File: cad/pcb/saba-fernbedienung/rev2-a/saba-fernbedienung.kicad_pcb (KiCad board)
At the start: 4 copper layers, 100 x 81.8 mm, 236 parts, among them J201 Conn_ARM_JTAG_SWD_10, J301 Conn_01x04, J302 Conn_01x04, J303 Micro_SD_Card, J304 Conn_01x04, J305 AudioJack3, J306 Conn_01x02, J307 Conn_01x04, J308 Conn_01x01, J309 Conn_01x01, J310 Conn_01x01, J311 Conn_01x04, J312 Conn_01x08, J313 USB_C_Receptacle_USB2.0, K601 G6K-2, K602 G6K-2, K603 G6K-2, K604 G6K-2, K605 G6K-2, K606 G6K-2, K607 EC2-5TNU, Q201 BC856, Q601 BC846, Q602 BC846, Q603 BC846, Q604 BC846, Q605 BC846, Q606 BC846, Q607 BC846, U201 DOIT-DEVKITV1-ESP32-WROOM-32, U301 TSOP31238, U401 TEC2-0911, U402 1117 1.8V, U403 1117 3.3V, U501 ADA4522-2, U502 LM339, U503 LTV-357T, U504 LTV-357T, U505 LTV-357T, U601 LTV-357T, U701 AD8656, U702 VS1053, Y701 12,288MHz

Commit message: ToDo-s bearbeitet
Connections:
- D601 pad 2: /Fernbedienung/Relais_Suchlauf_R -> /Fernbedienung/Relais_Suchlauf_L
- D606 pad 2: /Fernbedienung/Relais_Suchlauf_L -> /Fernbedienung/Relais_Suchlauf_R
- J312 pad 1: SPI_CS_LCD -> (no net)
- J312 pad 8: LCD_A0 -> (no net)
- K601 pad 2: /Fernbedienung/Relais_Leise -> /Fernbedienung/Relais_Laut
- K602 pad 8: /Fernbedienung/Relais_Suchlauf_R -> /Fernbedienung/Relais_Suchlauf_L
- K603 pad 2: /Fernbedienung/Relais_Laut -> /Fernbedienung/Relais_Leise
- K605 pad 8: /Fernbedienung/Relais_Suchlauf_L -> /Fernbedienung/Relais_Suchlauf_R
- Q601 pad 3: /Fernbedienung/Relais_Suchlauf_R -> /Fernbedienung/Relais_Suchlauf_L
- Q602 pad 3: /Fernbedienung/Relais_Laut -> /Fernbedienung/Relais_Leise
- Q603 pad 3: /Fernbedienung/Relais_Suchlauf_L -> /Fernbedienung/Relais_Suchlauf_R
- Q604 pad 3: /Fernbedienung/Relais_Leise -> /Fernbedienung/Relais_Laut
- R203 pad 2: Net-(R203-Pad2) -> (no net)
- R206 pad 2: SABA_Leise -> SABA_Laut
- R207 pad 2: SABA_Suchlauf_L -> SABA_Suchlauf_R
- R208 pad 2: SABA_Suchlauf_R -> SABA_Suchlauf_L
- R601 pad 2: SABA_Suchlauf_R -> SABA_Suchlauf_L
- R602 pad 2: SABA_Laut -> SABA_Leise
- R607 pad 2: SABA_Suchlauf_L -> SABA_Suchlauf_R
- R608 pad 2: SABA_Leise -> SABA_Laut
- U201 pad 11: SPI_MOSI -> (no net)
- U201 pad 15: LCD_A0 -> SPI_MOSI
- U201 pad 23: SPI_CS_LCD -> (no net)
- U201 pad 26: SABA_Suchlauf_L -> SABA_Suchlauf_R
- U201 pad 28: SABA_Suchlauf_R -> SABA_Suchlauf_L
- U201 pad 3: SABA_Leise -> SABA_Laut
- U201 pad 4: SABA_Laut -> SABA_Leise
- U201 pad 7: Net-(R203-Pad2) -> (no net)
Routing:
- net (no net): track 0.00 -> 48.4 mm, vias 0 -> 1
- net Net-(R203-Pad2): track 38.2 -> 0.00 mm, vias 1 -> 0
- net SPI_CS_LCD: track 10.2 -> 0.00 mm
- net SABA_Suchlauf_R: track 12.7 -> 22.2 mm
- net SABA_Suchlauf_L: track 22.2 -> 12.7 mm
- net /Fernbedienung/Relais_Suchlauf_R: track 7.08 -> 10.3 mm
- net /Fernbedienung/Relais_Suchlauf_L: track 10.3 -> 7.08 mm
- net /Fernbedienung/Relais_Leise: track 8.04 -> 5.70 mm
- net /Fernbedienung/Relais_Laut: track 5.70 -> 8.04 mm

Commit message: Change: Bauteilbezeichner
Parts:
- added C404: 10u, Capacitor_SMD:C_1206_3216Metric, F.Cu at (26.0, 138.8)
- added C714: 1u, Capacitor_SMD:C_0805_2012Metric, F.Cu at (63.6, 107.8)
- added C721: 1u, Capacitor_SMD:C_0805_2012Metric, F.Cu at (68.1, 107.8)
- added D201: 1N4148, Diode_SMD:D_SOD-323F, F.Cu at (50.3, 130.6)
- added D406: B140-E3, Diode_SMD:D_SMA, F.Cu at (39.4, 131.3)
- added D602: SMAJ33CA, Diode_SMD:D_SMA, F.Cu at (35.2, 123.2)
- added D605: SMAJ33CA, Diode_SMD:D_SMA, F.Cu at (27.2, 123.2)
- added K607: RT42xFxx, Relay_THT:Relay_DPDT_Schrack-RT2-FormC-Dual-Coil_RM5mm, F.Cu at (26.5, 117.3)
- added Q607: BC846, Package_TO_SOT_SMD:SOT-23, F.Cu at (41.5, 123.2)
- added R201: 10k, Resistor_SMD:R_0603_1608Metric, F.Cu at (54.4, 132.8)
- added R202: 0, Resistor_SMD:R_0603_1608Metric, F.Cu at (54.4, 130.3)
- added R622: 4k7, Resistor_SMD:R_0603_1608Metric, F.Cu at (56.1, 107.5)
- added R624: 10k, Resistor_SMD:R_0603_1608Metric, F.Cu at (56.1, 110.0)
- added R625: 4k7, Resistor_SMD:R_0603_1608Metric, F.Cu at (45.7, 122.2)
- added R722: 220, Resistor_SMD:R_0603_1608Metric, F.Cu at (67.4, 110.5)
- added R723: 220, Resistor_SMD:R_0603_1608Metric, F.Cu at (63.4, 110.5)
- added U401: 1117 5.0V, Package_TO_SOT_SMD:TO-252-3_TabPin2, F.Cu at (29.2, 133.1)
- R511, R519: value 68k -> 680k
- R512, R515, R529: value 1k -> 10k
- R513, R516, R530, R601, R602, R607, R608, R613, R614, R619: value 1k -> 4k7
- R514: value 27k -> 20k
- R520: value 470k -> 360k
- R521: value 3k3 -> 33k
- R525, R526, R536: value 22k -> 10k
- R528: value 15k -> 150k
- R533: value 18k -> 180k
- R534: value 8k2 -> 82k
- R604, R605, R610, R611, R615, R616: value 100k -> 4k7
- R618: value 5k7 -> 5k6
- R623: renamed from R622; value 1k -> 4k7
- R626: renamed from R623; value 100k -> 4k7
- renumbered C402 to C401, C403 to C402, C405 to C403, C407 to C405, C408 to C406, C410 to C407, C411 to C408, C412 to C409, C413 to C410, C414 to C411, C415 to C412, C416 to C413, C417 to C414, C418 to C415, C419 to C416, C714 to C715, C715 to C716, C716 to C718, C718 to C720, C720 to C722, C721 to C723, C722 to C724, C723 to C725, C724 to C726, C725 to C727, D406 to D407, D602 to D603, D603 to D604, D604 to D606, D605 to D607, D606 to D608, D607 to D609, D608 to D610, D609 to D611, D610 to D612, J313 to J312, L402 to L401, Q607 to Q608, R205 to R203, R206 to R204, R207 to R205, R208 to R206, R304 to R301, R305 to R302, R306 to R303, R307 to R304, R308 to R305, R711 to R710, R710 to R711, R715 to R712, R712 to R713, R713 to R714, R716 to R715, R717 to R716, R718 to R717, R714 to R718
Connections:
- C401 pad 1: Net-(C402-Pad1) -> Net-(C401-Pad1)
- C401 pad 2: Net-(C402-Pad2) -> GND
- C402 pad 1: Net-(C402-Pad1) -> Net-(C401-Pad1)
- C402 pad 2: Net-(C402-Pad2) -> GND
- C403 pad 2: Net-(C402-Pad2) -> GND
- C705 pad 1: Audio_Links -> /Audio/amp_links
- C718 pad 1: Audio_Rechts -> /Audio/amp_rechts
- D301 pad 1: Net-(D301-Pad1) -> Audio_Rechts
- D301 pad 2: Net-(D301-Pad2) -> Audio_Links
- D301 pad 3: GND -> Audio_GND
- D401 pad 1: Net-(C402-Pad1) -> Net-(C401-Pad1)
- D402 pad 1: Net-(C402-Pad1) -> Net-(C401-Pad1)
- D403 pad 2: Net-(C402-Pad2) -> GND
- D404 pad 2: Net-(C402-Pad2) -> GND
- D609 pad 1: Net-(D607-Pad1) -> +5V
- D609 pad 2: Net-(D607-Pad2) -> Net-(D609-Pad2)
- D610 pad 1: Net-(D608-Pad1) -> +5V
- D610 pad 2: Net-(D607-Pad2) -> Net-(D610-Pad2)
- J305 pad R: Net-(D301-Pad2) -> Audio_Rechts
- J305 pad S: Net-(D301-Pad1) -> Audio_GND
- J305 pad T: GND -> Audio_Links
- J308 pad 1: GND -> Audio_GND
- J309 pad 1: Net-(D301-Pad1) -> Audio_Rechts
- J310 pad 1: Net-(D301-Pad2) -> Audio_Links
- J311 pad 1: (no net) -> TA_Aktiv
- Q608 pad 3: Net-(D607-Pad2) -> Net-(D610-Pad2)
- R204 pad 2: Net-(R204-Pad2) -> (no net)
- R303 pad 1: Net-(D301-Pad2) -> (no net)
- R623 pad 2: SABA_Netz -> SABA_Netz_Reset
- R705 pad 1: GND -> Net-(C714-Pad2)
- R706 pad 2: Audio_Links -> /Audio/amp_links
- R714 pad 1: GND -> Net-(C721-Pad2)
- R718 pad 2: Audio_Rechts -> /Audio/amp_rechts
- U201 pad 11: (no net) -> SABA_Netz_Feedback
- U201 pad 16: ~RESET -> Net-(D201-Pad1)
- U201 pad 18: Net-(R204-Pad2) -> TA_Aktiv
- U201 pad 23: (no net) -> SABA_Netz_Reset
- U201 pad 24: SABA_Netz -> SABA_Netz_Set
- U201 pad 7: (no net) -> Net-(R202-Pad1)
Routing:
- net Net-(C402-Pad2): track 26.7 -> 0.00 mm
- net GND: track 171.5 -> 195.3 mm, vias 76 -> 73
- net Net-(C402-Pad1): track 14.0 -> 0.00 mm
- net Net-(C401-Pad1): track 0.00 -> 14.0 mm
- net Net-(C714-Pad2): track 0.00 -> 1.06 mm, vias 0 -> 1
- net Net-(C721-Pad2): track 0.00 -> 0.95 mm, vias 0 -> 1
- net Audio_GND: track 0.00 -> 0.92 mm, vias 0 -> 1
- removed copper zone on F.Cu, net Net-(C402-Pad1)
- removed copper zone on F.Cu, net Net-(C402-Pad2)

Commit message: Sicherung
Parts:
- added C201: 100n, Capacitor_SMD:C_0603_1608Metric, F.Cu at (43.6, 146.0)
- added C201: 100n, Capacitor_SMD:C_0603_1608Metric, F.Cu at (36.0, 156.6)
- added D202: 1N4148, Diode_SMD:D_SOD-323F, F.Cu at (50.8, 151.3)
- added Q201: BC846, Package_TO_SOT_SMD:SOT-23, F.Cu at (36.2, 153.1)
- added R203: 4k7, Resistor_SMD:R_0603_1608Metric, F.Cu at (53.5, 140.8)
- added R203: 10k, Resistor_SMD:R_0603_1608Metric, F.Cu at (34.1, 144.6)
- added R204: 10k, Resistor_SMD:R_0603_1608Metric, F.Cu at (47.6, 146.0)
- added R205: 1k, Resistor_SMD:R_0603_1608Metric, F.Cu at (53.5, 143.4)
- added R208: 4k7, Resistor_SMD:R_0603_1608Metric, F.Cu at (40.5, 152.1)
- added R209: 4k7, Resistor_SMD:R_0603_1608Metric, F.Cu at (40.5, 154.6)
- added T701: 1:1, local:Transformer_NF_EI14, F.Cu at (38.3, 94.0)
- added T702: 1:1, local:Transformer_NF_EI14, F.Cu at (53.9, 94.0)
- added U202: LTV-357T, Package_SO:SO-4_4.4x3.6mm_P2.54mm, F.Cu at (46.5, 142.2)
- renumbered R203 to R206, R204 to R207, R205 to R208, R206 to R209
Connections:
- U201 pad 18: TA_Aktiv -> Net-(C201-Pad2)

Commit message: Sicherung
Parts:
- removed the C201 at (36.0, 156.6)
- removed the C401 at (174.6, 65.2)
- removed the C404 at (26.0, 138.8)
- removed the C404 at (196.0, 72.0)
- removed the C406 at (161.0, 71.0)
- removed the C409 at (174.6, 79.3)
- removed the D201 at (115.7, 120.9)
- removed D301: 5V, Package_TO_SOT_SMD:SOT-323_SC-70
- removed the J312 at (111.2, 119.0)
- removed the J312 at (153.3, 62.5)
- removed the K607 at (26.5, 117.3)
- removed the K607 at (187.5, 94.8)
- removed the L401 at (191.2, 66.5)
- removed Q201: BC846, Package_TO_SOT_SMD:SOT-23
- removed Q201: BC856, Package_TO_SOT_SMD:SOT-23
- removed the R203 at (34.1, 144.6)
- removed the R203 at (103.8, 106.5)
- removed the R204 at (47.6, 146.0)
- removed the R204 at (114.0, 118.0)
- removed the R208 at (40.5, 152.1)
- removed the R209 at (40.5, 154.6)
- removed the R301 at (140.9, 79.4)
- removed the R302 at (140.9, 77.9)
- removed the R303 at (151.5, 70.0)
- removed the R303 at (140.9, 80.9)
- removed the U401 at (29.2, 133.1)
- removed the U401 at (182.0, 71.0)
- added C404: 10u, Capacitor_SMD:C_1206_3216Metric, F.Cu at (189.4, 79.6)
- added J312: USB_C_Receptacle_USB2.0, Connector_USB:USB_C_Receptacle_HRO_TYPE-C-31-M-12, F.Cu at (182.7, 62.5)
- added K607: RT42xFxx, Relay_THT:Relay_DPDT_Schrack-RT2-FormC-Dual-Coil_RM5mm, F.Cu at (194.4, 116.7)
- added R204: 10k, Resistor_SMD:R_0603_1608Metric, F.Cu at (139.9, 166.3)
- added R303: 5k1, Resistor_SMD:R_0603_1608Metric, F.Cu at (180.9, 70.0)
- added U401: 1117 5.0V, Package_TO_SOT_SMD:TO-252-3_TabPin2, F.Cu at (191.4, 84.4)
- C402: footprint Capacitor_THT:CP_Radial_D10.0mm_P5.00mm -> local:CP_Radial_D10.0mm_P5.00mm_L20.00mm_liegend
- C405: footprint local:CP_Radial_D10.0mm_P5.00mm_liegend -> local:CP_Radial_D10.0mm_P5.00mm_L12.50mm_liegend
- moved Q607 176.0 mm to (217.4, 129.8)
- moved R625 176.0 mm to (221.6, 128.8)
- moved R622 166.6 mm to (221.9, 123.9)
- moved R624 162.3 mm to (217.8, 124.5)
- moved D605 141.3 mm to (168.2, 113.8), turned to 180 degrees
- moved D602 133.6 mm to (168.2, 110.3)
- moved U202 116.1 mm to (162.1, 153.6)
- moved T701 108.8 mm to (145.6, 75.9), turned to 270 degrees
- moved T702 108.3 mm to (160.7, 75.9), turned to 270 degrees
- moved D202 100.3 mm to (149.8, 167.1)
- moved C201 100.3 mm to (142.6, 161.8)
- moved R203 100.3 mm to (152.4, 156.7)
- moved R205 100.3 mm to (152.4, 159.2)
- moved R723 82.6 mm to (141.0, 82.1)
- moved R722 79.4 mm to (141.0, 80.6)
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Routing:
- net SABA_Netz: track 97.2 -> 0.00 mm
- net SABA_Netz_Set: track 0.00 -> 88.6 mm
- net GND: track 195.3 -> 140.8 mm, vias 73 -> 70
- net (no net): track 48.4 -> 0.00 mm, vias 1 -> 0
- net Net-(D609-Pad2): track 0.00 -> 42.4 mm, vias 0 -> 1
- net LCD_A0: track 34.3 -> 0.00 mm
- net Audio_GND: track 0.92 -> 32.9 mm, vias 1 -> 0
- net /Audio/amp_rechts: track 0.00 -> 27.8 mm
- net Net-(D607-Pad2): track 22.6 -> 0.00 mm
- net Audio_Links: track 4.00 -> 26.1 mm
- net SPI_SCK: track 68.2 -> 47.2 mm
- net Net-(D301-Pad1): track 19.0 -> 0.00 mm
- net SABA_Lautstaerke: track 27.3 -> 43.7 mm, vias 0 -> 1
- net Net-(D301-Pad2): track 15.6 -> 0.00 mm
- net Net-(D607-Pad1): track 13.2 -> 0.00 mm
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- added copper zone on B.Cu, net +5V
- removed copper zone on F.Cu, net Net-(C401-Pad1)
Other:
- outline, holes or cut-outs redrawn
- board text added: "REV 2"
- board text removed: "REV 1"

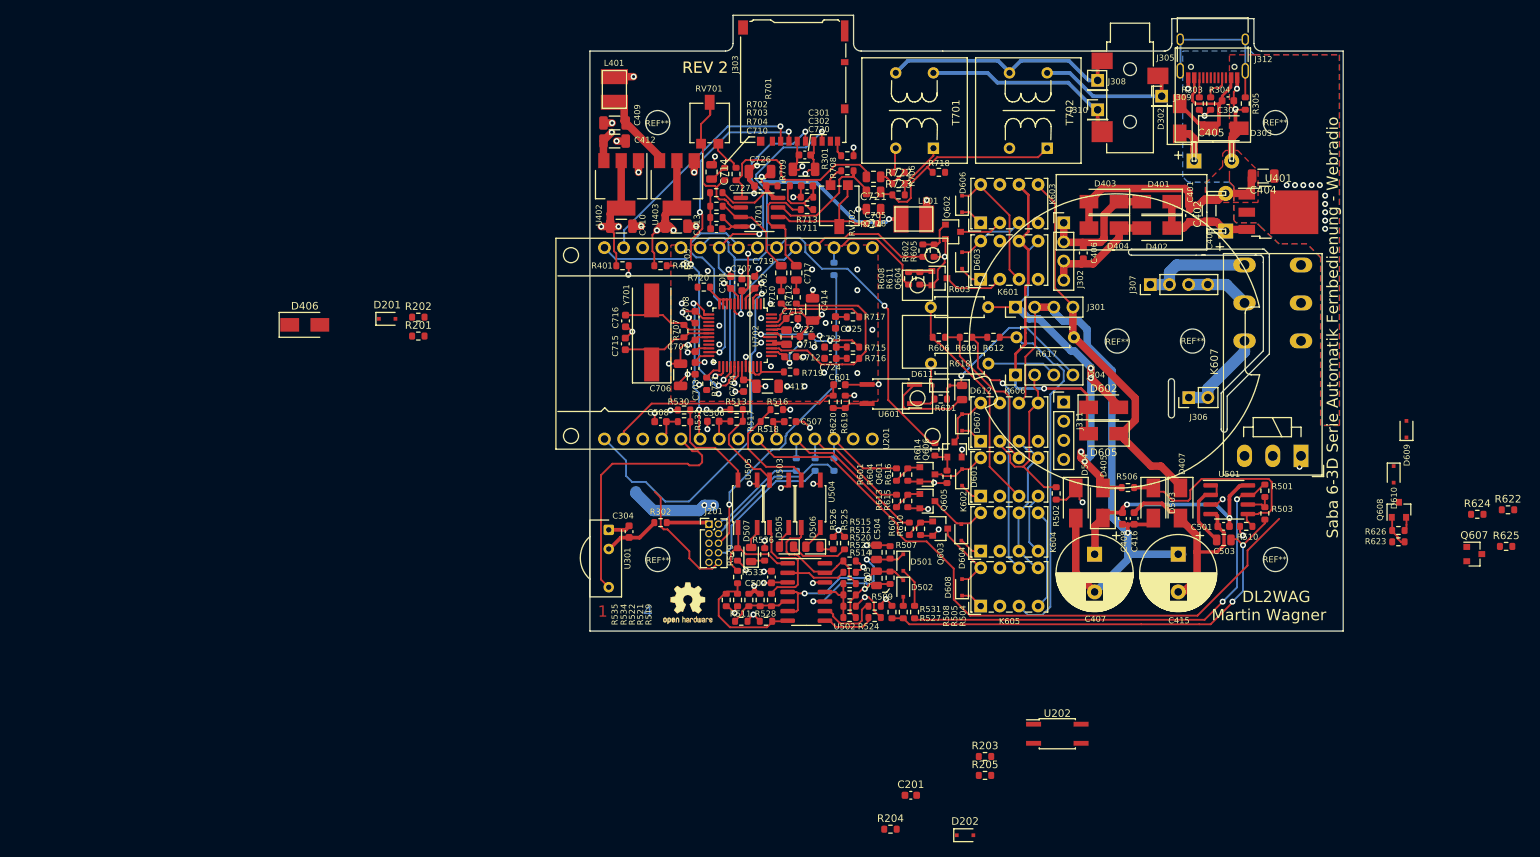
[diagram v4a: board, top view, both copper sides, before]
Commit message: alle Bauteile platziert
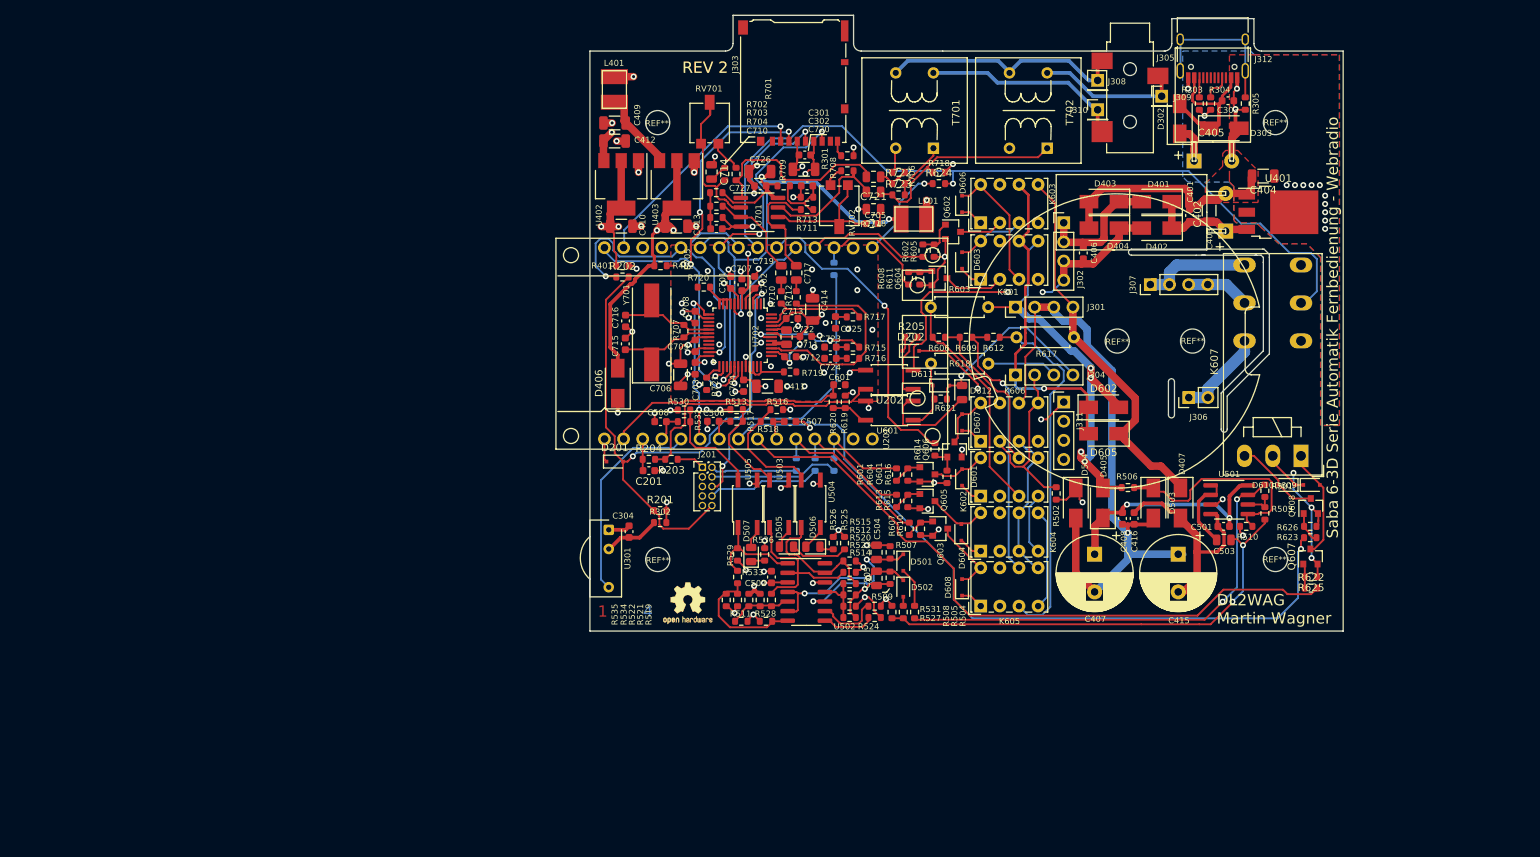
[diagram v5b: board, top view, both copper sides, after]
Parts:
- moved R624 83.9 mm to (146.3, 80.6)
- moved D202 64.7 mm to (142.6, 102.8)
- moved R205 59.0 mm to (142.7, 101.0)
- moved R204 58.6 mm to (107.8, 117.2)
- moved R203 57.3 mm to (110.8, 117.2), turned to 180 degrees
- moved C201 55.4 mm to (107.8, 118.7), turned to 180 degrees
- moved U202 52.0 mm to (139.8, 106.6), turned to 180 degrees
- moved D406 42.3 mm to (103.7, 107.1), turned to 90 degrees
- moved R201 39.6 mm to (109.3, 124.0)
- moved D201 35.7 mm to (103.3, 117.5)
- moved R622 28.1 mm to (195.7, 134.3)
- moved R202 27.6 mm to (104.3, 93.0)
- moved R625 26.2 mm to (195.7, 132.8), turned to 180 degrees
- moved Q607 21.8 mm to (195.7, 130.1), turned to 90 degrees
- moved D609 14.6 mm to (195.8, 120.6), turned to 0 degrees
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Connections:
- U201 pad 11: SABA_Netz_Feedback -> Net-(R202-Pad1)
- U201 pad 7: Net-(R202-Pad1) -> SABA_Netz_Feedback
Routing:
- net SABA_Netz_Feedback: track 0.53 -> 106.5 mm, vias 0 -> 1
- net SABA_Netz_Reset: track 0.00 -> 99.8 mm, vias 0 -> 1
- net GND: track 140.8 -> 215.4 mm, vias 70 -> 75
- net +5V: track 130.3 -> 78.2 mm, vias 15 -> 13
- net Net-(R203-Pad2): track 0.00 -> 34.8 mm
- net Earth: track 17.9 -> 47.2 mm, vias 0 -> 2
- net Net-(D609-Pad2): track 42.4 -> 14.6 mm, vias 1 -> 0
- net TA_Aktiv: track 0.00 -> 24.9 mm, vias 0 -> 2
- net Net-(R202-Pad1): track 0.00 -> 20.4 mm, vias 0 -> 1
- net ~RESET: track 65.4 -> 83.8 mm, vias 1 -> 2
- net +3.3VA: track 37.0 -> 53.9 mm
- net +3V3: track 47.8 -> 63.3 mm, vias 11 -> 14
- net Net-(D610-Pad2): track 0.00 -> 11.4 mm
- net Net-(R205-Pad2): track 0.00 -> 9.01 mm
- net IR_RX: track 34.2 -> 27.6 mm
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- added copper zone on In1.Cu, net (none)

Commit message: sicherung
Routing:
- net +5V: track 78.2 -> 133.6 mm, vias 13 -> 18
- net +3V3: track 63.3 -> 78.5 mm
- net SABA_Lautstaerke: track 43.7 -> 45.8 mm
- net Net-(R714-Pad2): track 18.0 -> 19.6 mm
- net SPI_CS_SDCARD: track 30.8 -> 29.4 mm
- net SPI_MISO: track 54.1 -> 53.1 mm
- net SPI_MOSI: track 64.0 -> 63.0 mm
- net GND: track 215.4 -> 216.0 mm, vias 75 -> 79
- added copper zone on In2.Cu, net GND
- removed copper zone on In1.Cu, net (none)
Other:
- outline, holes or cut-outs redrawn

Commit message: Controller Rev2 fertig
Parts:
- R511: value 680k -> 270k
- R519: value 680k -> 470k
- R521: value 33k -> 22k
- moved REF** 0.30 mm to (113.0, 136.6) (x2)
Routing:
- net GND: track 216.0 -> 259.2 mm
- net +5V: track 133.6 -> 164.6 mm
- added copper zone on B.Cu, net GND
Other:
- board text added: "Hardware: https://github.com/martin-wagner/saba-6-3d-fernbedienung-hw Software: https://github.com/martin-wagner/ESP32-Radio"
